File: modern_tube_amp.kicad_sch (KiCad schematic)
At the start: 91 parts, among them J1 XLR, J2 RCA, J3 Conn_01x02_Socket, J4 Conn_01x02_Socket, J5 connector to power board (mol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, J6 Conn_01x02_Socket, SW1 SW_Push, SW2 SW_SPST, T1 Transformer_Audio, T2 Transformer_Audio, T3 Transformer_Audio, T4 1650RA, U1 74HC14, U3 12ax7, U4 CD4066BM96, U5 kt88, U6 kt88, U7 LM317_BIAS

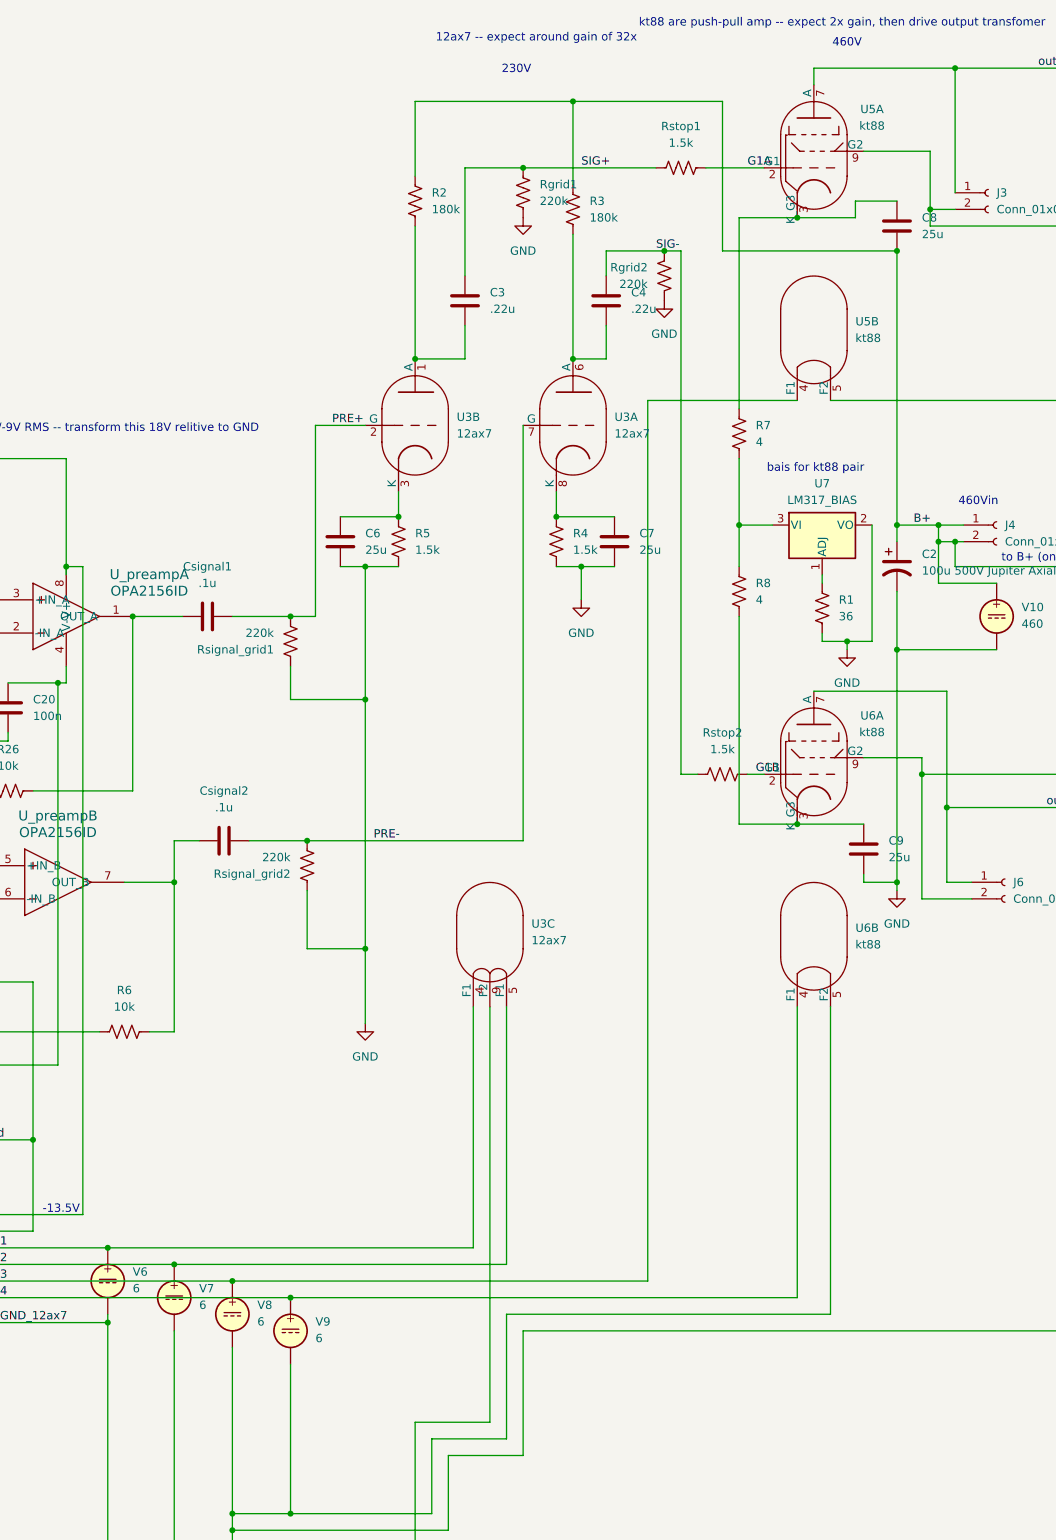
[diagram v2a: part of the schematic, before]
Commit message: PMOS buffer to bias output of 12ax7
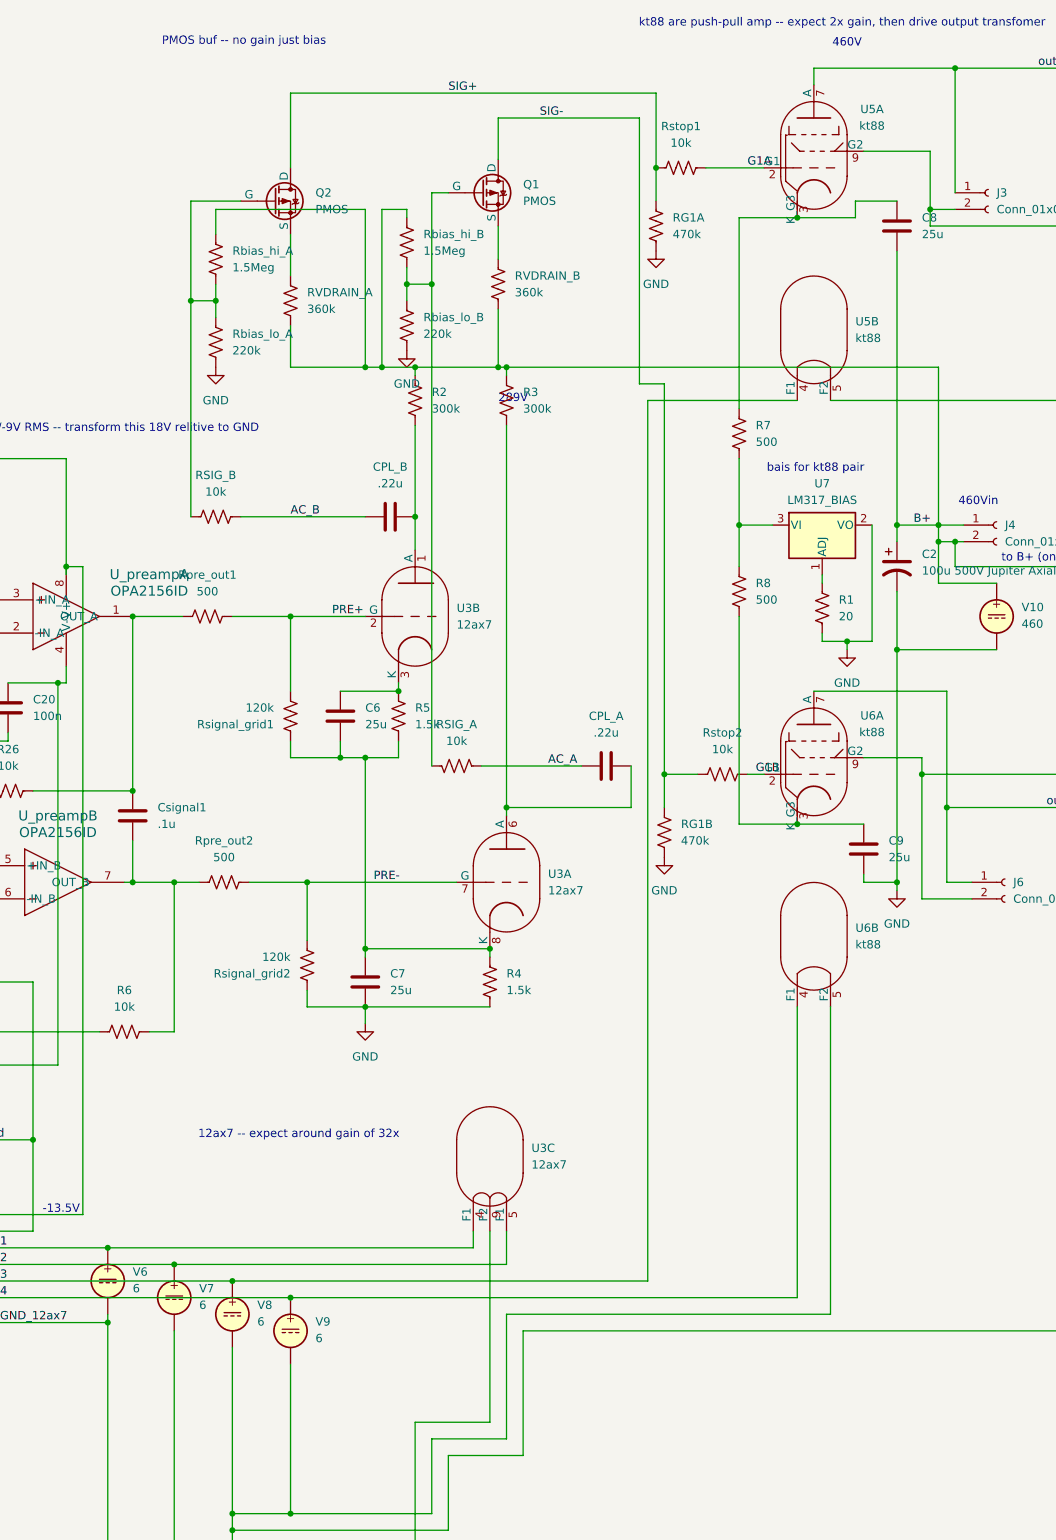
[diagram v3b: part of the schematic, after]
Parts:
- removed Csignal2: .1u, symbol Device:C
- added Q1, Q2: PMOS, symbol Simulation_SPICE:PMOS
- added RG1A, RG1B: 470k, symbol Device:R_US
- added RVDRAIN_A, RVDRAIN_B: 360k, symbol Device:R_US
- added Rbias_hi_A, Rbias_hi_B: 1.5Meg, symbol Device:R_US
- added Rbias_lo_A, Rbias_lo_B: 220k, symbol Device:R_US
- added Rpre_out1, Rpre_out2: 500, symbol Device:R_US
- R1: value 36 -> 20
- R2, R3: value 180k -> 300k
- R7, R8: value 4 -> 500
- RSIG_A: renamed from Rgrid2; value 220k -> 10k
- RSIG_B: renamed from Rgrid1; value 220k -> 10k
- Rsignal_grid1, Rsignal_grid2: value 220k -> 120k
- Rstop1, Rstop2: value 1.5k -> 10k
- renumbered C4 to CPL_A, C3 to CPL_B
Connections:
- net B+: now also RVDRAIN_A.2, RVDRAIN_B.2, Rbias_hi_A.1, Rbias_hi_B.1
- net GND: now also RG1A.2, RG1B.2, Rbias_lo_A.2, Rbias_lo_B.2; no longer C6.2, R5.2, RSIG_A.1, RSIG_B.2, Rsignal_grid1.1
- net PRE+: now also Rpre_out1.2; no longer Csignal1.2
- net PRE-: now also Rpre_out2.2
- net SIG+: now also Q2.1 (D), RG1A.1; no longer CPL_B.1, RSIG_B.1
- net SIG-: now also Q1.1 (D), RG1B.1; no longer CPL_A.1, RSIG_A.2
- net at R6.2, U_preamp.7 (OUT_B): now also Csignal1.2, Rpre_out2.1
- net at C7.1, R4.1, U3.8 (K): now also C6.2, R5.2, Rsignal_grid1.1
- net at Csignal1.1, R26.2, U_preamp.1 (OUT_A): now also Rpre_out1.1
- new net: Q1.2 (G), RSIG_A.2, Rbias_hi_B.2, Rbias_lo_B.1
- new net: Q2.2 (G), RSIG_B.1, Rbias_hi_A.2, Rbias_lo_A.1
- new net: Q1.3 (S), RVDRAIN_B.1
- new net: Q2.3 (S), RVDRAIN_A.1
- new net AC_A: CPL_A.1, RSIG_A.1
- new net AC_B: CPL_B.1, RSIG_B.2
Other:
- note added: "289V"
- note added: "PMOS buf -- no gain just bias"
- note removed: "230V"
- moved on the sheet: C6, C7, CPL_A, CPL_B, R2, R3, R4, R5, RSIG_A, RSIG_B, Rsignal_grid1, Rsignal_grid2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
